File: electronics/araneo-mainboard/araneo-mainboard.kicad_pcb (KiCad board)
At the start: 2 copper layers, 39 parts, among them J1 Conn_01x03_Pin, J10 Diode2, J11 Diode3, J12 OLED, J2 Conn_01x03_Pin, J3 Conn_01x03_Pin, J4 Conn_01x03_Pin, J5 Conn_01x03_Pin, J6 Conn_01x03_Pin, J7 Conn_01x03_Pin, J8 Conn_01x03_Pin, J9 Diode1, SW1 SW_SPST, U1 module_mpu6050, U2 L78M05CDT, U3 BD9C601EFJ

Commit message: electronics: full PCB
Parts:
- added ?: LOGO, Custom:konar, F.Cu at (145.0, 128.5)
- added POWER1: Conn_01x02_Pin, Connector_AMASS:AMASS_XT30U-M_1x02_P5.0mm_Vertical, F.Cu at (98.0, 68.0)
- C5: value C -> OPEN; moved to B.Cu
- C8: value C -> 1.5nF; moved to B.Cu
- R1: value R -> 1.2k; moved to B.Cu
- R2: value R -> 7.8k; moved to B.Cu
- R3: value R -> 39k; moved to B.Cu
- SW1: value SW_SPST -> SW
- moved R1 26.5 mm to (104.6, 77.5), turned to 0 degrees
- moved R2 25.3 mm to (104.6, 79.0), turned to 180 degrees
- moved R3 21.4 mm to (105.0, 85.5), turned to 90 degrees
- moved C8 18.4 mm to (103.5, 85.5)
- moved C5 13.5 mm to (104.6, 80.5), turned to 180 degrees
- moved R6 9.77 mm to (153.0, 119.0)
- moved F1 8.32 mm to (105.6, 72.4)
- moved R5 7.43 mm to (149.5, 119.0)
- moved S3 6.53 mm to (107.5, 104.0)
- moved C4 6.18 mm to (111.0, 79.5), turned to 180 degrees
- moved S1 6.03 mm to (103.0, 104.0)
- moved C3 5.36 mm to (110.9, 77.5), turned to 180 degrees
- moved R4 4.47 mm to (146.0, 119.0)
- moved OLED1 4.37 mm to (153.6, 122.0)
- moved SW1 4.30 mm to (118.0, 78.0), turned to -90 degrees
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- renumbered U1 to IMU1, J9 to LED1, J10 to LED2, J11 to LED3, J12 to OLED1, J1 to S1, J2 to S2, J3 to S3, J4 to S4, J5 to S5, J6 to S6, J7 to S7, J8 to S8
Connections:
- C8 pad 1: Net-(U3-COMP) -> Net-(C8-Pad1)
- C8 pad 2: Net-(C8-Pad2) -> GND
- R3 pad 1: Net-(C8-Pad2) -> Net-(U3-COMP)
- R3 pad 2: GND -> Net-(C8-Pad1)
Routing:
- net +6V: track 0.00 -> 120.2 mm, vias 0 -> 1
- net +7.4V: track 0.00 -> 62.3 mm
- net PWM2: track 0.00 -> 57.1 mm, vias 0 -> 1
- net PWM6: track 0.00 -> 48.9 mm
- net PWM1: track 0.00 -> 48.0 mm, vias 0 -> 1
- net +3V3: track 0.00 -> 46.0 mm
- net PWM4: track 0.00 -> 45.3 mm, vias 0 -> 1
- net PWM5: track 0.00 -> 39.2 mm, vias 0 -> 2
- net PWM3: track 0.00 -> 38.1 mm, vias 0 -> 1
- net D3: track 0.00 -> 37.6 mm, vias 0 -> 1
- net PWM8: track 0.00 -> 36.4 mm, vias 0 -> 2
- net D2: track 0.00 -> 33.5 mm, vias 0 -> 1
- net D1: track 0.00 -> 32.6 mm, vias 0 -> 1
- net EN: track 0.00 -> 30.3 mm, vias 0 -> 2
- net PWM7: track 0.00 -> 28.2 mm
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- added copper zone on B.Cu, net GND
- added copper zone on F.Cu, net GND
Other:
- board outline added: 68.5 x 74 mm
- board text added: "15.07.2026 Projekt inżynierski prowadzony przez Mateusza Cholewińskiego"
- board text added: "Michał Sadecki Araneo Project KoNaR"

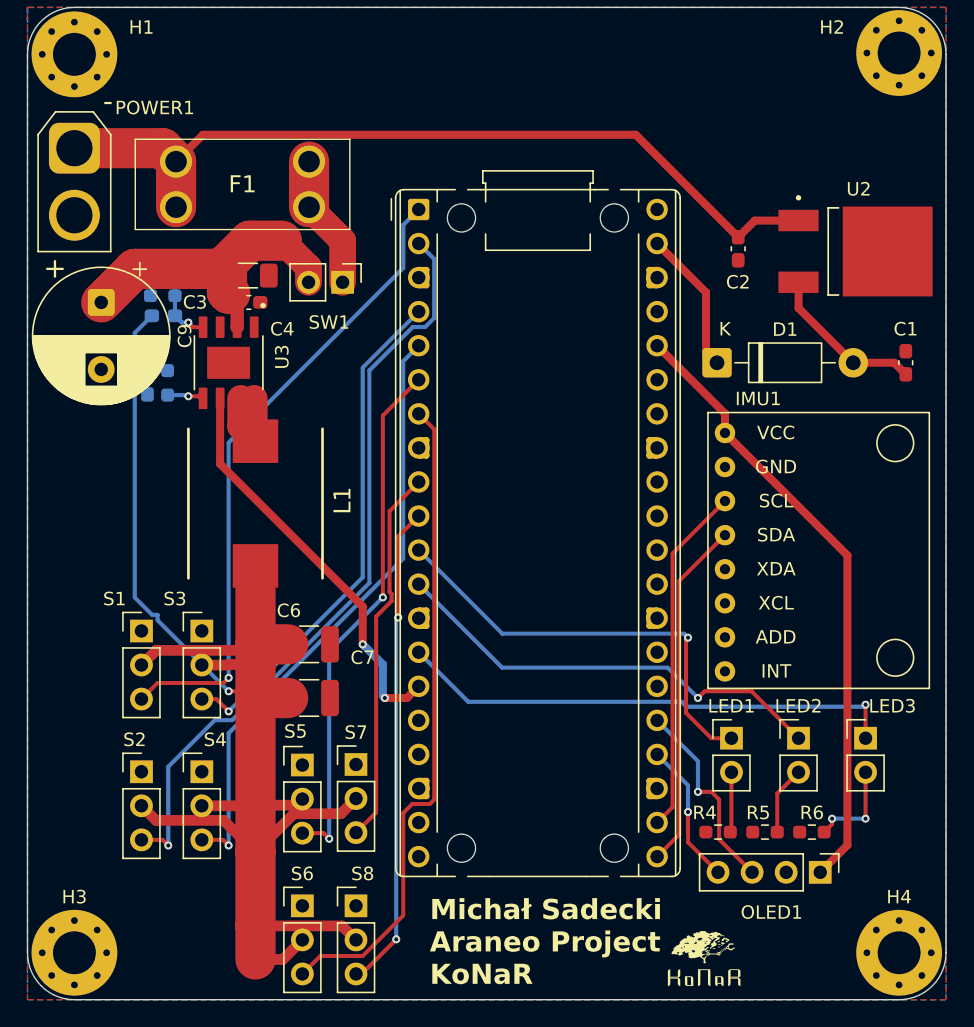
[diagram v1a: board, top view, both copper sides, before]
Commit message: electronics: add pin labels on pcb
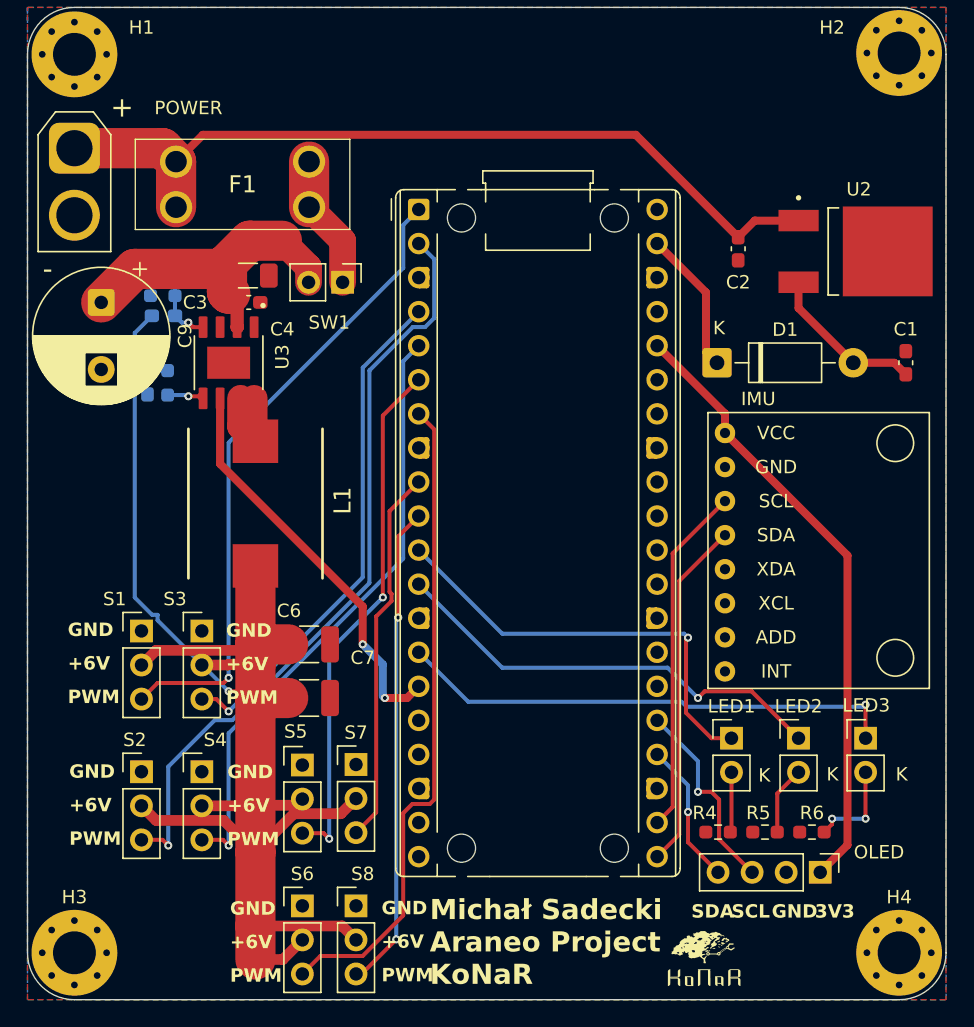
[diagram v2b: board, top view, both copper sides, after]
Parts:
- renumbered IMU1 to IMU, OLED1 to OLED, POWER1 to POWER
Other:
- board text added: "+6V"
- board text added: "3V3"
- board text added: "GND"
- board text added: "K"
- board text added: "PWM"
- board text added: "SCL"
- board text added: "SDA"

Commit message: electronics: fix schematic and prepare for wiring
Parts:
- removed C9: 470uF, Capacitor_THT:CP_Radial_D10.0mm_P5.00mm
- moved ? 43.7 mm to (188.5, 132.5)
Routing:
- net Net-(SW1-B): track 23.6 -> 13.7 mm

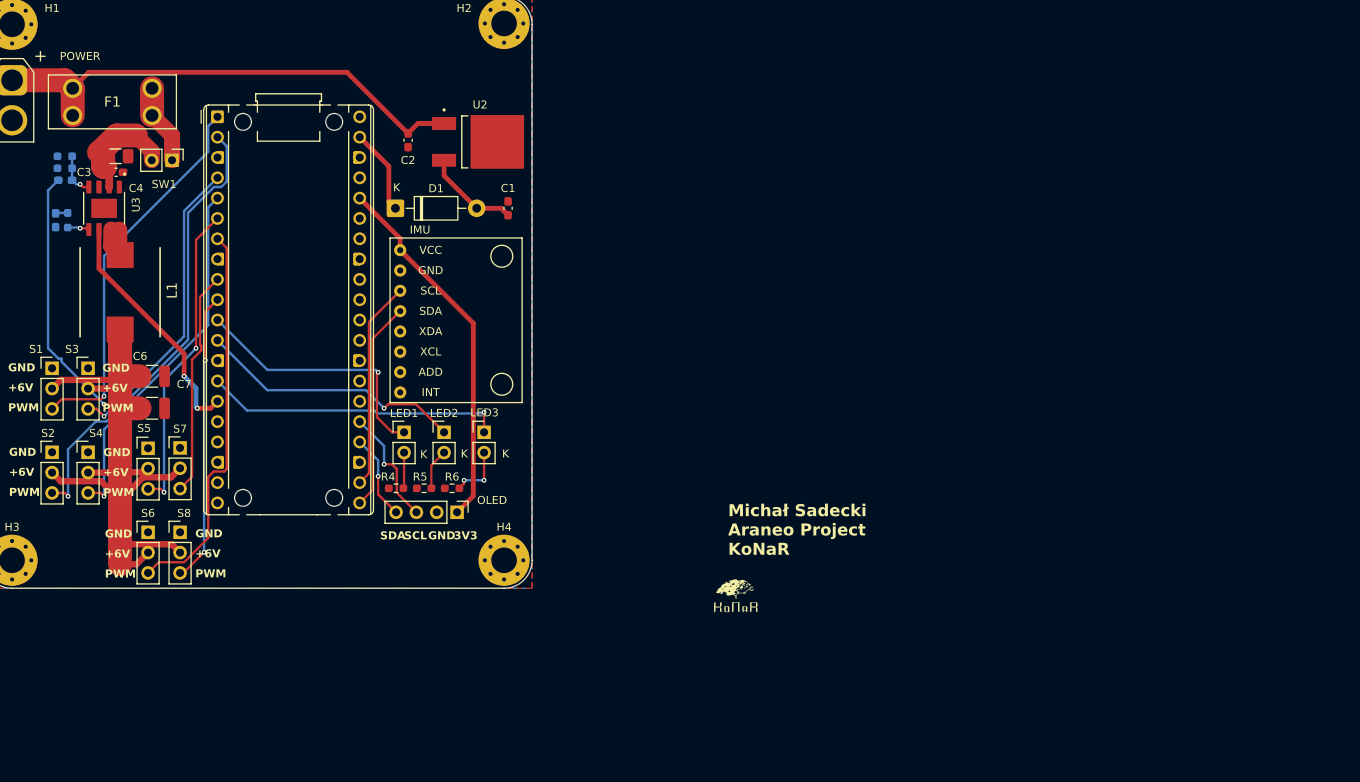
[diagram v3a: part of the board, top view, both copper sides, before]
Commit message: electronics: add speaker
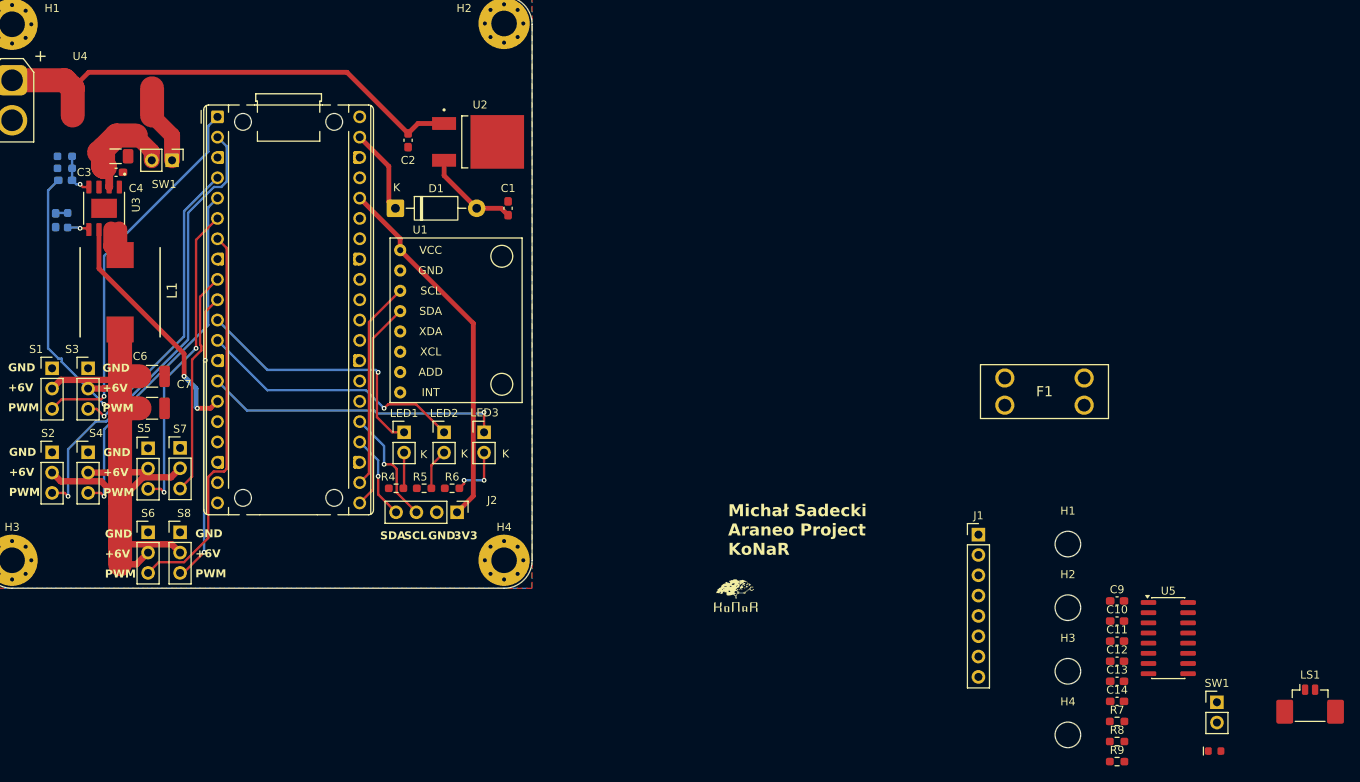
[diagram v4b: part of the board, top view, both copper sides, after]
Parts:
- added C10: 100nF, Capacitor_SMD:C_0603_1608Metric_Pad1.08x0.95mm_HandSolder, F.Cu at (236.1, 135.6)
- added C11: 220pF, Capacitor_SMD:C_0603_1608Metric_Pad1.08x0.95mm_HandSolder, F.Cu at (236.1, 138.1)
- added C12: 220pF, Capacitor_SMD:C_0603_1608Metric_Pad1.08x0.95mm_HandSolder, F.Cu at (236.1, 140.6)
- added C13: 470nF, Capacitor_SMD:C_0603_1608Metric_Pad1.08x0.95mm_HandSolder, F.Cu at (236.1, 143.1)
- added C14: 470nF, Capacitor_SMD:C_0603_1608Metric_Pad1.08x0.95mm_HandSolder, F.Cu at (236.1, 145.6)
- added C9: 100nF, Capacitor_SMD:C_0603_1608Metric_Pad1.08x0.95mm_HandSolder, F.Cu at (236.1, 133.1)
- added D2: POWER_LED, PCM_SparkFun-LED:LED_0603_1608Metric, F.Cu at (248.3, 151.8)
- added H1: MountingHole, MountingHole:MountingHole_3.2mm_M3, F.Cu at (230.0, 126.0)
- added H2: MountingHole, MountingHole:MountingHole_3.2mm_M3, F.Cu at (230.0, 133.9)
- added H3: MountingHole, MountingHole:MountingHole_3.2mm_M3, F.Cu at (230.0, 141.9)
- added H4: MountingHole, MountingHole:MountingHole_3.2mm_M3, F.Cu at (230.0, 149.8)
- added J1: GPIO, Connector_PinHeader_2.54mm:PinHeader_1x08_P2.54mm_Vertical, F.Cu at (218.8, 124.8)
- added LS1: Speaker, Connector_Molex:Molex_PicoBlade_53398-0271_1x02-1MP_P1.25mm_Vertical, F.Cu at (260.3, 145.4)
- added R7: 4.7k, Resistor_SMD:R_0603_1608Metric_Pad0.98x0.95mm_HandSolder, F.Cu at (236.1, 148.1)
- added R8: 100, Resistor_SMD:R_0603_1608Metric_Pad0.98x0.95mm_HandSolder, F.Cu at (236.1, 150.7)
- added R9: 4.7k, Resistor_SMD:R_0603_1608Metric_Pad0.98x0.95mm_HandSolder, F.Cu at (236.1, 153.2)
- added SW1: SW, Connector_PinHeader_2.54mm:PinHeader_1x02_P2.54mm_Vertical, F.Cu at (248.6, 145.7)
- added U5: PAM8403D, Package_SO:SOIC-16_3.9x9.9mm_P1.27mm, F.Cu at (242.5, 137.7)
- A1: value RaspberryPi_Pico_W -> RaspberryPi_Pico_2W
- R4, R5, R6: value 330 -> 4.7k
- S1: value Conn_01x03_Pin -> Servo1
- S2: value Conn_01x03_Pin -> Servo2
- S3: value Conn_01x03_Pin -> Servo3
- S4: value Conn_01x03_Pin -> Servo4
- S5: value Conn_01x03_Pin -> Servo5
- S6: value Conn_01x03_Pin -> Servo6
- S7: value Conn_01x03_Pin -> Servo7
- S8: value Conn_01x03_Pin -> Servo8
- U1: renamed from IMU; value module_mpu6050 -> IMU
- U4: renamed from POWER; value Conn_01x02_Pin -> POWER
- moved F1 122.0 mm to (222.1, 108.6)
- renumbered OLED to J2
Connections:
- net +3V3 renamed /+3V3
- net +5V_LDO renamed /+5V_LDO
- net +6V renamed /+6V
- net D1 renamed /D1
- net D2 renamed /D2
- net D3 renamed /D3
- net EN renamed /EN
- net PWM1 renamed /PWM1
- net PWM2 renamed /PWM2
- net PWM3 renamed /PWM3
- net PWM4 renamed /PWM4
- net PWM5 renamed /PWM5
- net PWM6 renamed /PWM6
- net PWM7 renamed /PWM7
- net PWM8 renamed /PWM8
- net SCL_IMU renamed /SCL_IMU
- net SCL_OLED renamed /SCL_OLED
- net SDA_IMU renamed /SDA_IMU
- net SDA_OLED renamed /SDA_OLED
- A1 pad 16: unconnected-(A1-GPIO12-Pad16) -> /GPIO12
- A1 pad 17: unconnected-(A1-GPIO13-Pad17) -> /GPIO13
- A1 pad 19: unconnected-(A1-GPIO14-Pad19) -> /GPIO14
- A1 pad 20: unconnected-(A1-GPIO15-Pad20) -> /GPIO15
- A1 pad 26: unconnected-(A1-GPIO20-Pad26) -> /SPEAKER
- A1 pad 27: unconnected-(A1-GPIO21-Pad27) -> /SHDN
- A1 pad 29: unconnected-(A1-GPIO22-Pad29) -> /GPIO22
- A1 pad 31: unconnected-(A1-GPIO26_ADC0-Pad31) -> /GPIO26
- A1 pad 32: unconnected-(A1-GPIO27_ADC1-Pad32) -> /GPIO27
- A1 pad 34: unconnected-(A1-GPIO28_ADC2-Pad34) -> /GPIO28
- A1 pad 35: unconnected-(A1-ADC_VREF-Pad35) -> /+3V3_RC
- C3 pad 2: Net-(SW1-B) -> +7.4V
- C4 pad 2: Net-(SW1-B) -> +7.4V
- F1 pad 1: +7.4V -> Net-(SW1-B)
- F1 pad 2: Net-(SW1-A) -> +7.4V
- U3 pad 2: Net-(SW1-B) -> +7.4V

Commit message: electronics: add footprints
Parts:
- removed the H1 at (98.0, 61.0)
- removed the H2 at (159.5, 60.9)
- removed the H3 at (98.0, 128.0)
- removed the H4 at (159.5, 128.0)
- removed the SW1 at (118.0, 78.0)
- added C15: 1uF, Capacitor_SMD:C_0603_1608Metric_Pad1.08x0.95mm_HandSolder, F.Cu at (174.4, 87.0)
- added C16: 1uF, Capacitor_SMD:C_0603_1608Metric_Pad1.08x0.95mm_HandSolder, F.Cu at (174.4, 89.5)
- added C17: 470uF, Capacitor_THT:CP_Radial_D10.0mm_P5.00mm, F.Cu at (147.6, 55.0)
- added C18: 1uF, Capacitor_SMD:C_0603_1608Metric_Pad1.08x0.95mm_HandSolder, F.Cu at (174.4, 92.0)
- added FB1: FerriteBead, Resistor_SMD:R_0603_1608Metric_Pad0.98x0.95mm_HandSolder, F.Cu at (156.9, 76.0)
- added FB2: FerriteBead, Resistor_SMD:R_0603_1608Metric_Pad0.98x0.95mm_HandSolder, F.Cu at (155.4, 79.0)
- C2: footprint Capacitor_SMD:C_0603_1608Metric_Pad1.08x0.95mm_HandSolder -> Capacitor_SMD:C_0805_2012Metric_Pad1.18x1.45mm_HandSolder
- C5, C8, R1, R3: moved to F.Cu
- LS1: footprint Connector_Molex:Molex_PicoBlade_53398-0271_1x02-1MP_P1.25mm_Vertical -> PCM_SparkFun-Connector:ScrewTerminal_1x02_P3.5mm_Blue
- R2: value 7.8k -> 7.87k; moved to F.Cu
- moved H1 163.6 mm to (89.0, 43.0)
- moved SW1 159.0 mm to (119.5, 53.0)
- moved H3 146.3 mm to (85.5, 119.0)
- moved F1 129.7 mm to (103.6, 55.9)
- moved LS1 117.7 mm to (157.5, 88.0), turned to 90 degrees
- moved U5 109.8 mm to (157.0, 68.9)
- moved H2 102.9 mm to (179.0, 44.5)
- moved D2 102.7 mm to (158.8, 101.5)
- moved J1 83.1 mm to (146.5, 83.9)
- moved C12 83.0 mm to (168.5, 92.5)
- moved C9 83.0 mm to (168.5, 84.9)
- moved R7 83.0 mm to (168.5, 100.0)
- moved C10 83.0 mm to (168.5, 87.5)
- moved C11 83.0 mm to (168.5, 90.0)
- moved C13 83.0 mm to (168.5, 95.0)
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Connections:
- C9 pad 1: /+3V3 -> GND
- U5 pad 6: unconnected-(U5-VDD-Pad6) -> Net-(U5-VDD)
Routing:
- net /+6V: track 120.2 -> 0.00 mm, vias 1 -> 0
- net +7.4V: track 62.3 -> 0.00 mm
- net /PWM2: track 57.1 -> 0.00 mm, vias 1 -> 0
- net /PWM6: track 48.9 -> 0.00 mm
- net /PWM1: track 48.0 -> 0.00 mm, vias 1 -> 0
- net /+3V3: track 46.0 -> 0.00 mm
- net /PWM4: track 45.3 -> 0.00 mm, vias 1 -> 0
- net /PWM5: track 39.2 -> 0.00 mm, vias 2 -> 0
- net /PWM3: track 38.1 -> 0.00 mm, vias 1 -> 0
- net /D3: track 37.6 -> 0.00 mm, vias 1 -> 0
- net /PWM8: track 36.4 -> 0.00 mm, vias 2 -> 0
- net /D2: track 33.5 -> 0.00 mm, vias 1 -> 0
- net /D1: track 32.6 -> 0.00 mm, vias 1 -> 0
- net /EN: track 30.3 -> 0.00 mm, vias 2 -> 0
- net /PWM7: track 28.2 -> 0.00 mm
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- removed copper zone on B.Cu, net GND
- removed copper zone on F.Cu, net GND
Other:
- board outline removed
- board text removed: "+6V"
- board text removed: "3V3"
- board text removed: "GND"
- board text removed: "K"
- board text removed: "PWM"
- board text removed: "SCL"
- board text removed: "SDA"

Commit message: electronics: pcb v2
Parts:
- moved ? 96.2 mm to (120.0, 43.0)
- moved C8 73.1 mm to (99.0, 61.5)
- moved R4 73.0 mm to (94.5, 89.0), turned to 180 degrees
- moved R3 71.3 mm to (99.0, 60.0), turned to 180 degrees
- moved C3 67.6 mm to (121.5, 49.5), turned to 180 degrees
- moved R6 66.7 mm to (103.0, 101.0), turned to -90 degrees
- moved C2 64.2 mm to (157.0, 45.0), turned to 90 degrees
- moved C6 62.2 mm to (119.0, 70.5), turned to 90 degrees
- moved C7 61.7 mm to (119.0, 76.0), turned to -90 degrees
- moved C5 60.0 mm to (105.0, 58.0), turned to 180 degrees
- moved R2 59.9 mm to (105.0, 56.5), turned to 180 degrees
- moved LED1 56.6 mm to (94.5, 94.5), turned to 180 degrees
- moved D2 56.0 mm to (159.5, 45.5), turned to -90 degrees
- moved R7 54.9 mm to (161.5, 45.5), turned to -90 degrees
- moved R1 54.5 mm to (109.5, 58.0), turned to 180 degrees
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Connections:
- A1 pad 11: /D1 -> /GPIO8
- A1 pad 12: /D2 -> /GPIO9
- A1 pad 14: /D3 -> /GPIO10
- A1 pad 17: /GPIO13 -> /D1
- A1 pad 19: /GPIO14 -> /D2
- A1 pad 20: /GPIO15 -> /D3
- A1 pad 21: /SDA_IMU -> /GPIO16
- A1 pad 22: /SCL_IMU -> /GPIO17
- A1 pad 31: /GPIO26 -> /SDA_IMU
- A1 pad 32: /GPIO27 -> /SCL_IMU
- C2 pad 1: +7.4V -> /+7.4V_F
- C3 pad 2: +7.4V -> /+7.4V_F
- C4 pad 2: +7.4V -> /+7.4V_F
- D2 pad 2: +7.4V -> /+7.4V_F
- J1 pad 1: /GPIO12 -> /GPIO8
- J1 pad 2: /GPIO13 -> /GPIO9
- J1 pad 3: /GPIO14 -> /GPIO10
- J1 pad 4: /GPIO15 -> /GPIO12
- J1 pad 5: /GPIO22 -> /GPIO16
- J1 pad 6: /GPIO26 -> /GPIO17
- J1 pad 7: /GPIO27 -> /GPIO22
- SW1 pad 1: +7.4V -> /+7.4V_F
- U2 pad 1: +7.4V -> /+7.4V_F
- U3 pad 2: +7.4V -> /+7.4V_F
- U4 pad 1: +7.4V -> /+7.4V_F
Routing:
- net /+7.4V_F: track 0.00 -> 60.1 mm
- net /PWM6: track 0.00 -> 44.4 mm
- net /PWM1: track 0.00 -> 42.2 mm, vias 0 -> 1
- net /GPIO28: track 0.00 -> 37.5 mm
- net /PWM8: track 0.00 -> 37.3 mm, vias 0 -> 1
- net /PWM5: track 0.00 -> 35.4 mm
- net /PWM7: track 0.00 -> 35.2 mm, vias 0 -> 1
- net /+3V3: track 0.00 -> 33.7 mm, vias 0 -> 1
- net /PWM4: track 0.00 -> 33.3 mm
- net /D1: track 0.00 -> 33.0 mm
- net /PWM2: track 0.00 -> 31.5 mm
- net /PWM3: track 0.00 -> 31.3 mm
- net Net-(C11-Pad2): track 0.00 -> 29.4 mm
- net /+6V: track 0.00 -> 26.6 mm, vias 0 -> 2
- net /GPIO8: track 0.00 -> 25.2 mm, vias 0 -> 1
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- added copper zone on F.Cu, net /+6V
- added copper zone on F.Cu, net /+7.4V_F
- added copper zone on F.Cu, net Net-(L1-Pad1)
- added copper zone on F.Cu, net Net-(SW1-B)
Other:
- board outline added: 71.5 x 68.5 mm
- board text added: "GPIO"
- board text added: "OLED"
- board text added: "SPEAKER"
